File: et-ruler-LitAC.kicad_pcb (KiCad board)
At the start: 2 copper layers, 166 x 28 mm, 27 parts, among them J1 Conn_01x03, J3 Pmod-Interface-GPIO6, J4 Pmod-Interface-GPIO6, J5 AudioJack3_SwitchTR, SW1 SW_DPDT, U1 OP07

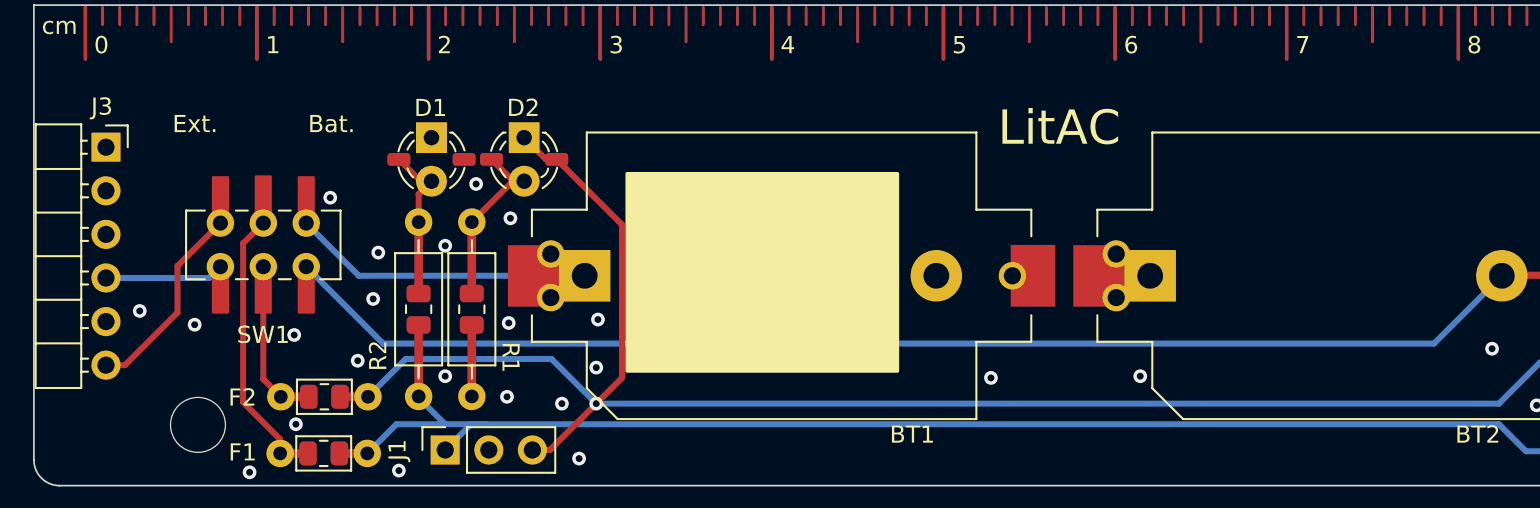
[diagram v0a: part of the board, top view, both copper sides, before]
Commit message: Fix pitch for SW1 footprint
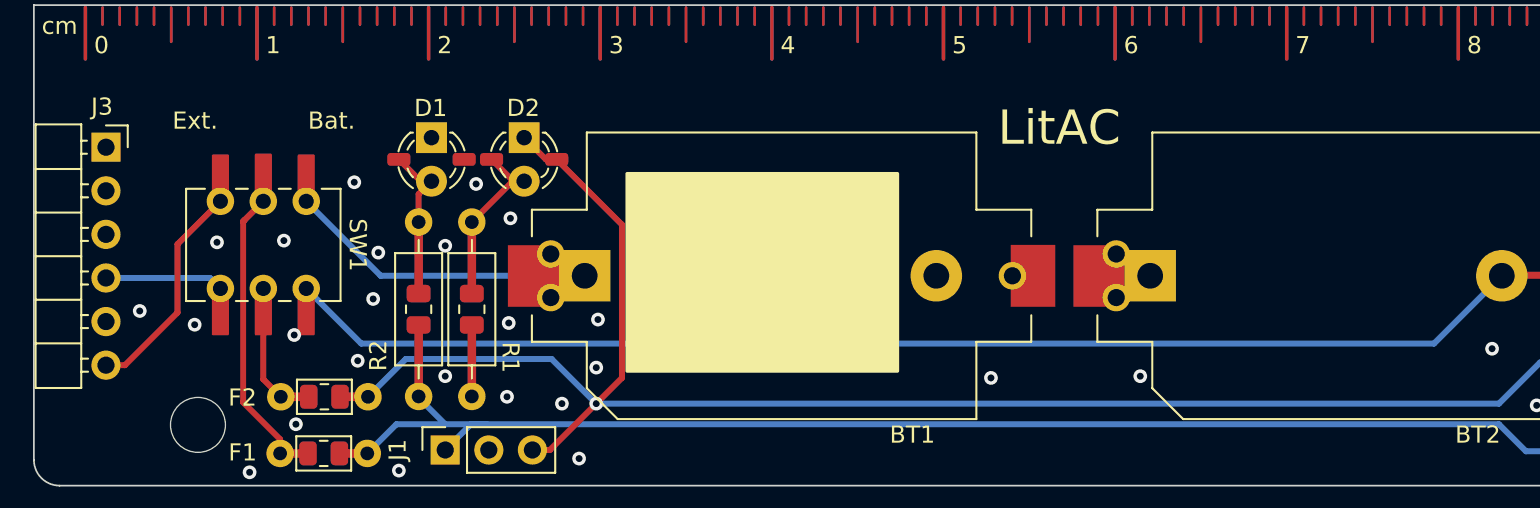
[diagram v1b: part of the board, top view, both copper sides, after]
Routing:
- net Net-(SW1-B): track 14.8 -> 16.1 mm
- net V+_ext_in: track 11.7 -> 13.0 mm
- net Net-(BT2--): track 83.0 -> 82.5 mm
- net Net-(BT1-+): track 19.0 -> 19.5 mm
- net GND: vias 48 -> 50

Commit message: Bump to version 1.1
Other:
- board text added: "1.1"
- board text removed: "1.0"
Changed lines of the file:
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@@
   (gr_line (start 50.532 89.278) (end 213.532 89.278)
     (stroke (width 0.1) (type solid)) (layer "Edge.Cuts"))
-  (gr_text "1.0" (at 210.4 88.4) (layer "F.Cu" knockout)
+  (gr_text "1.1" (at 210.4 88.4) (layer "F.Cu" knockout)
     (effects (font (size 1.5 1.5) (thickness 0.3) bold) (justify left bottom))
   )
